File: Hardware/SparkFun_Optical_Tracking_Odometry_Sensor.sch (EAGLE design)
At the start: 49 parts, among them J1 QWIIC_RIGHT_ANGLE, J2 QWIIC_RIGHT_ANGLE, Q1 100mA/20V/3.8Ω, Q2 100mA/20V/3.8Ω, U1 PAA5160E1-Q, U2 LSM6DS0, U3 STM32C011F6U6, U4 RT9080-18GJ5

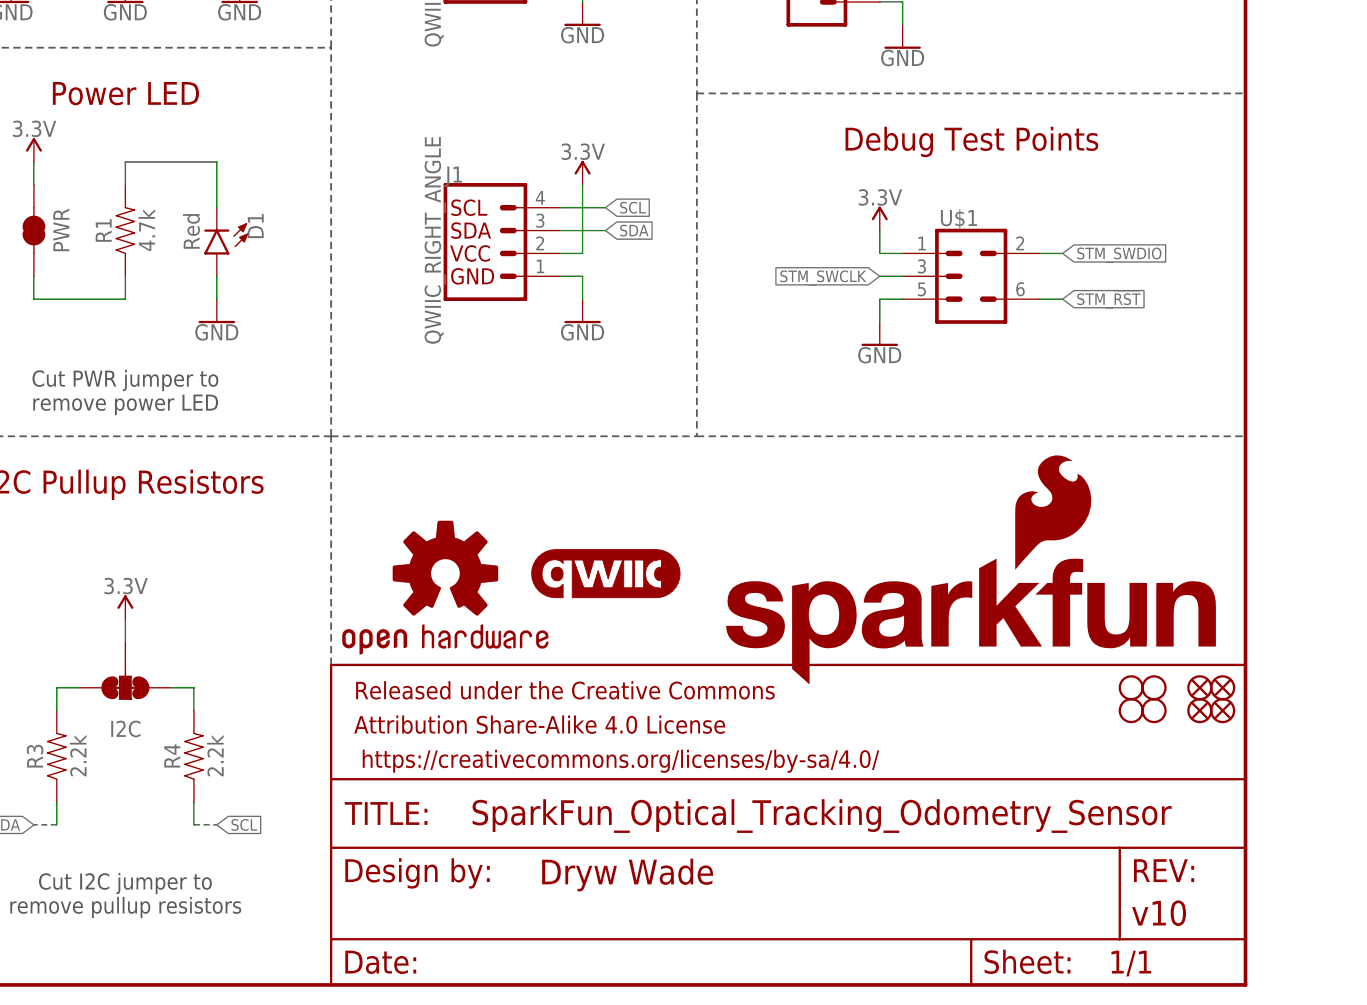
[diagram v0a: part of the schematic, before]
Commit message: v11 updates
Bump version number to v11
Fix PAA5160 footprint (pad pitch was 0.6mm instead of 0.65mm, and needed to be pushed out 0.1mm)
Fix power LED orientation (doh!)
Fix measures
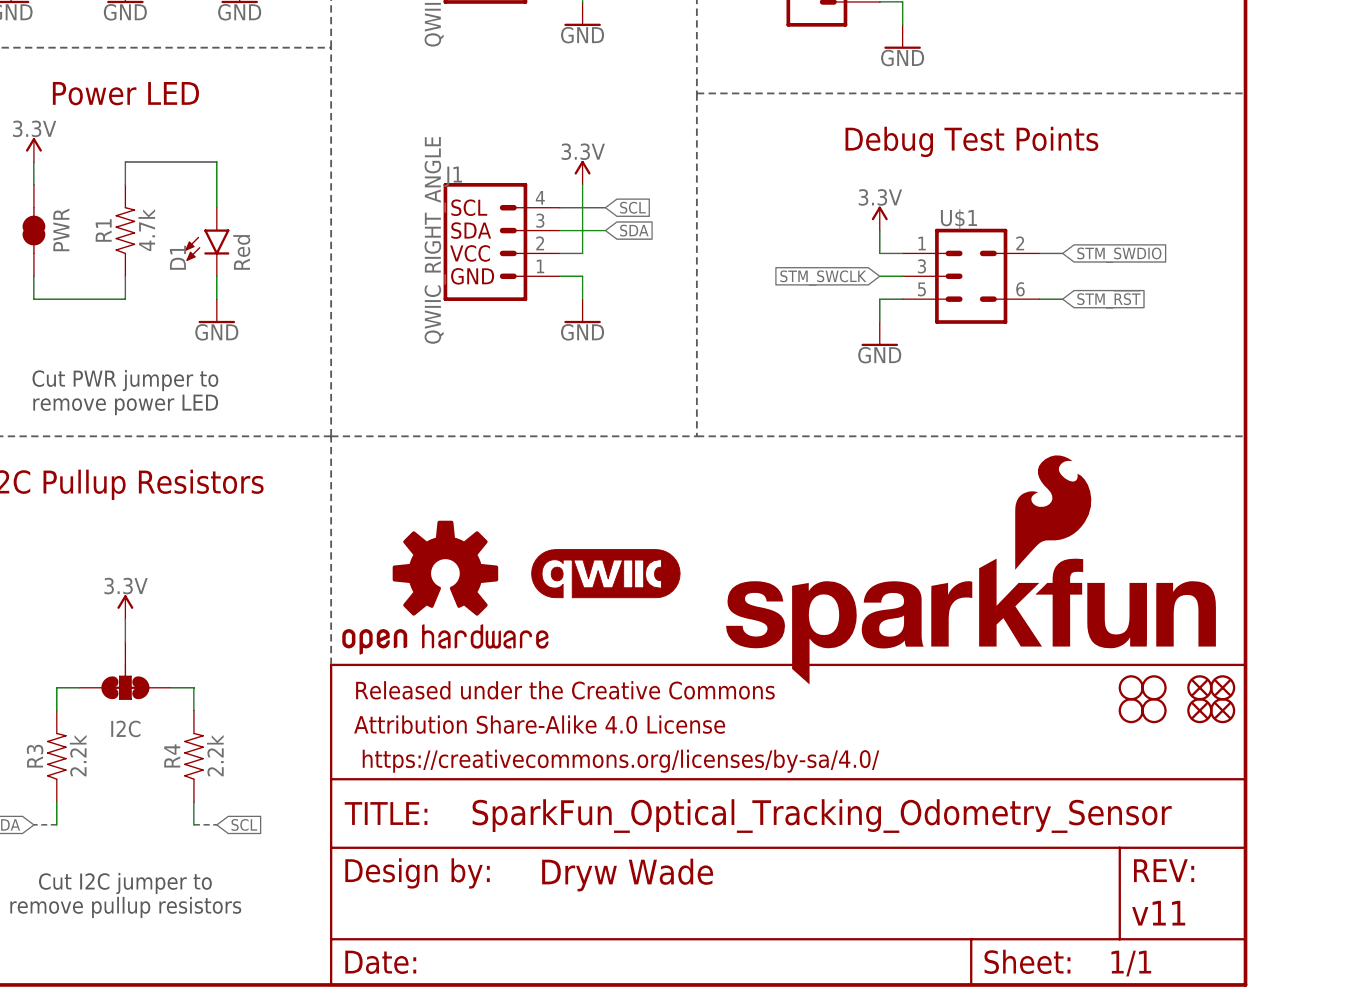
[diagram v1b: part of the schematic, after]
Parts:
- FRAME1: REV v10 -> v11
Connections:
- net GND: now also D1.C; no longer D1.A
- net N$2: now also D1.A; no longer D1.C
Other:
- moved on the sheet: D1
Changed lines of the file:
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@@
 <part name="FRAME1" library="SparkFun-Aesthetics" deviceset="FRAME-LETTER" device="">
 <attribute name="DESIGNER" value="Dryw Wade"/>
-<attribute name="REV" value="v10"/>
+<attribute name="REV" value="v11"/>
 </part>
 <part name="U1" library="Optical_Tracking_Odometry_Sensor" deviceset="PAA5160E1-Q" device=""/>
@@
 <instance part="FD3" gate="G$1" x="243.84" y="30.48" smashed="yes"/>
 <instance part="FD4" gate="G$1" x="243.84" y="33.02" smashed="yes"/>
-<instance part="D1" gate="G$1" x="134.62" y="81.28" smashed="yes" rot="R180">
-<attribute name="NAME" x="138.049" y="85.852" size="1.778" layer="95" font="vector" rot="R270"/>
-<attribute name="VALUE" x="132.715" y="85.852" size="1.778" layer="96" font="vector" rot="R270" align="top-left"/>
+<instance part="D1" gate="G$1" x="134.62" y="83.82" smashed="yes">
+<attribute name="NAME" x="131.191" y="79.248" size="1.778" layer="95" font="vector" rot="R90"/>
+<attribute name="VALUE" x="136.525" y="79.248" size="1.778" layer="96" font="vector" rot="R90" align="top-left"/>
 </instance>
 <instance part="R1" gate="G$1" x="124.46" y="83.82" smashed="yes" rot="R90">
@@
 </segment>
 <segment>
-<pinref part="D1" gate="G$1" pin="A"/>
-<pinref part="GND8" gate="1" pin="GND"/>
-<wire x1="134.62" y1="78.74" x2="134.62" y2="76.2" width="0.1524" layer="91"/>
-</segment>
-<segment>
 <pinref part="GND26" gate="1" pin="GND"/>
 <wire x1="20.32" y1="124.46" x2="20.32" y2="127" width="0.1524" layer="91"/>
 <pinref part="C14" gate="G$1" pin="2"/>
+</segment>
+<segment>
+<pinref part="GND8" gate="1" pin="GND"/>
+<pinref part="D1" gate="G$1" pin="C"/>
+<wire x1="134.62" y1="76.2" x2="134.62" y2="78.74" width="0.1524" layer="91"/>
 </segment>
 </net>
@@
 <pinref part="R1" gate="G$1" pin="2"/>
 <wire x1="124.46" y1="88.9" x2="124.46" y2="91.44" width="0.1524" layer="91"/>
-<pinref part="D1" gate="G$1" pin="C"/>
 <wire x1="124.46" y1="91.44" x2="134.62" y2="91.44" width="0.1524" layer="91"/>
-<wire x1="134.62" y1="91.44" x2="134.62" y2="86.36" width="0.1524" layer="91"/>
-</segment>
-</net>
+<pinref part="D1" gate="G$1" pin="A"/>
+<wire x1="134.62" y1="86.36" x2="134.62" y2="91.44" width="0.1524" layer="91"/>
+</segment>
+</net>

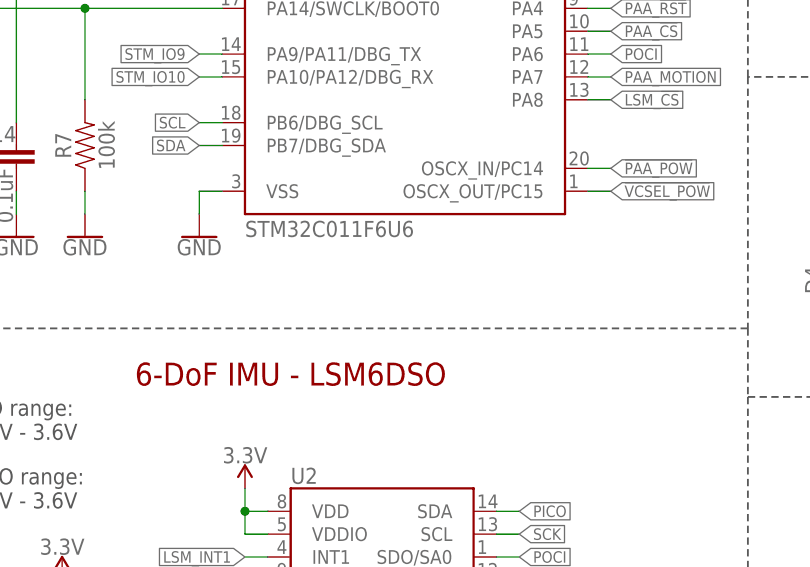
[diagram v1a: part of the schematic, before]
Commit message: Add default I2C address to schematic
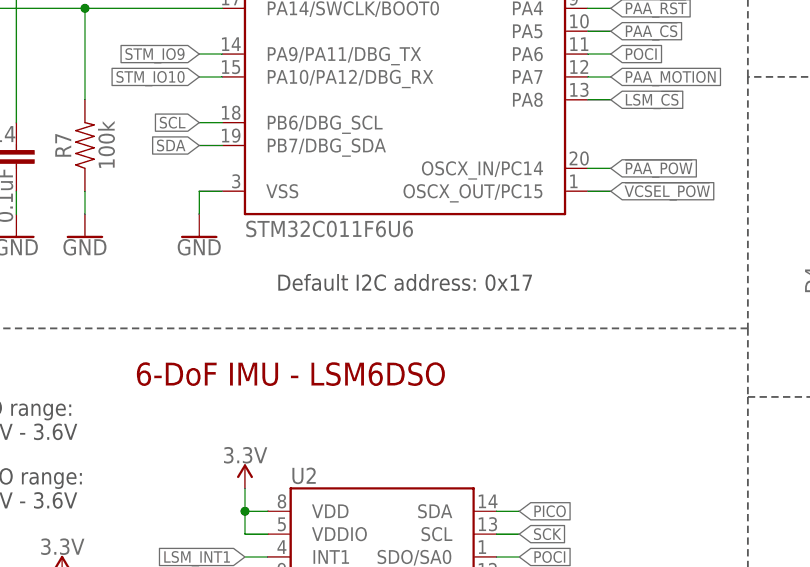
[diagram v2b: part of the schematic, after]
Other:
- note added: "Default I2C address: 0x17"
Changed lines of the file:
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@@
 voltage range:
 2.8V - 3.3V</text>
+<text x="63.5" y="116.84" size="1.778" layer="97" font="vector" align="center">Default I2C address: 0x17</text>
 </plain>
 <instances>
